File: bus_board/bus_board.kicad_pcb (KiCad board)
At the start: 2 copper layers, 150 x 30 mm, 20 parts, among them J5 Conn_02x08_Odd_Even, J6 Conn_02x08_Odd_Even, J7 Conn_02x08_Odd_Even, J8 Conn_02x08_Odd_Even

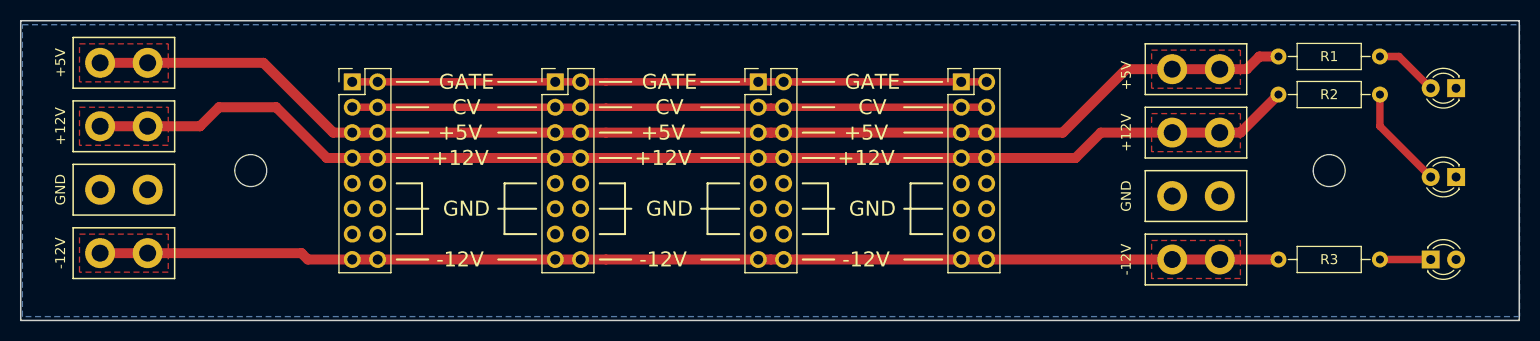
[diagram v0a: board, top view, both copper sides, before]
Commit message: added fuse holder
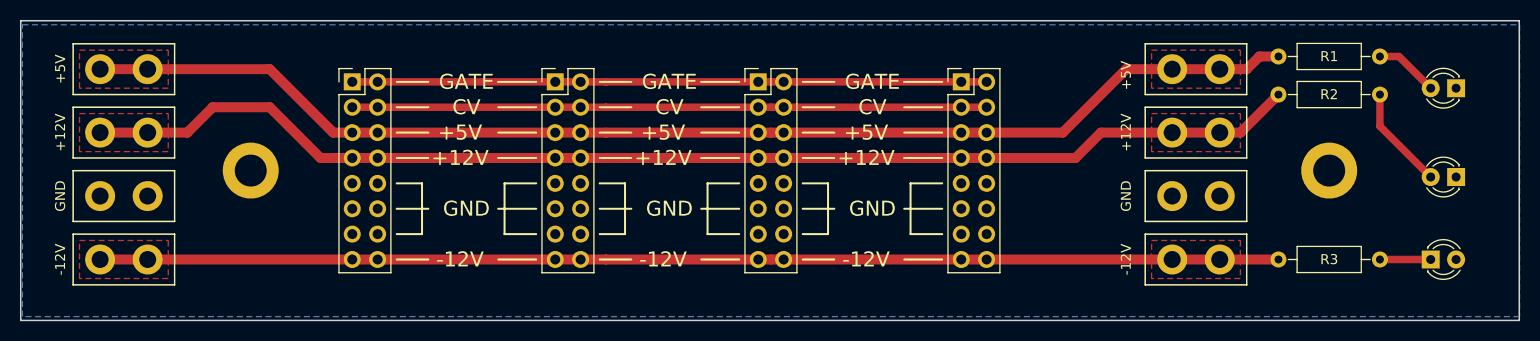
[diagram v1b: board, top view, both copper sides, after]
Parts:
- removed the REF** at (73.0, 80.0)
- removed the REF** at (181.0, 80.0)
- added REF**: MountingHole_3.2mm_M3_DIN965_Pad, Mounting_Holes:MountingHole_3.2mm_M3_DIN965_Pad, F.Cu at (181.0, 80.0)
- added REF**: MountingHole_3.2mm_M3_DIN965_Pad, Mounting_Holes:MountingHole_3.2mm_M3_DIN965_Pad, F.Cu at (73.0, 80.0)
- moved +12V 0.64 mm to (60.3, 77.5)
- moved +5V 0.64 mm to (60.3, 71.1)
- moved -12V 0.64 mm to (60.3, 90.2)
- moved GND 0.63 mm to (60.3, 83.8)
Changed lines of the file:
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@@
     (thickness 1.6)
     (drawings 79)
-    (tracks 70)
+    (tracks 68)
     (zones 0)
     (modules 20)
@@
     (visible_elements 7FFFFFFF)
     (pcbplotparams
-      (layerselection 0x010fc_ffffffff)
+      (layerselection 0x010f0_ffffffff)
       (usegerberextensions false)
       (usegerberattributes false)
@@
       (plotinvisibletext false)
       (padsonsilk false)
-      (subtractmaskfromsilk false)
+      (subtractmaskfromsilk true)
       (outputformat 1)
       (mirror false)
-      (drillshape 1)
+      (drillshape 0)
       (scaleselection 1)
-      (outputdirectory ""))
+      (outputdirectory "GERBERS/"))
   )
   (net 0 "")
@@
     (add_net /-12V)
   )
+  (module Mounting_Holes:MountingHole_3.2mm_M3_DIN965_Pad (layer F.Cu)
+    (at 180.975 80)
+    (descr "Mounting Hole 3.2mm, M3, DIN965")
+    (tags "mounting hole 3.2mm m3 din965")
+    (attr virtual)
+    (fp_text reference REF** (at 0 -3.8) (layer F.SilkS) hide
+      (effects (font (size 1 1) (thickness 0.15)))
+    )
+    (fp_text value MountingHole_3.2mm_M3_DIN965_Pad (at 0 3.8) (layer F.Fab)
+      (effects (font (size 1 1) (thickness 0.15)))
+    )
+    (fp_text user %R (at 0.3 0) (layer F.Fab)
+      (effects (font (size 1 1) (thickness 0.15)))
+    )
+    (fp_circle (center 0 0) (end 2.8 0) (layer Cmts.User) (width 0.15))
+    (fp_circle (center 0 0) (end 3.05 0) (layer F.CrtYd) (width 0.05))
+    (pad 1 thru_hole circle (at 0 0) (size 5.6 5.6) (drill 3.2) (layers *.Cu *.Mask))
+  )
   (module Pin_Headers:Pin_Header_Straight_2x08_Pitch2.54mm (layer F.Cu)
     (at 83.185 71.12)
@@
   )
   (module digikey-footprints:spade_connector (layer F.Cu)
-    (at 60.325 76.835)
+    (at 60.325 77.47)
     (fp_text reference +12V (at -6.35 -1.27 90) (layer F.SilkS)
       (effects (font (size 1 1) (thickness 0.15)))
@@
   )
   (module digikey-footprints:spade_connector (layer F.Cu)
-    (at 60.325 70.485)
+    (at 60.325 71.12)
     (fp_text reference +5V (at -6.35 -1.27 90) (layer F.SilkS)
       (effects (font (size 1 1) (thickness 0.15)))
@@
   )
   (module digikey-footprints:spade_connector (layer F.Cu)
-    (at 60.325 89.535)
+    (at 60.325 90.17)
     (fp_text reference -12V (at -6.35 -1.27 90) (layer F.SilkS)
       (effects (font (size 1 1) (thickness 0.15)))
@@
   )
   (module digikey-footprints:spade_connector (layer F.Cu)
-    (at 60.325 83.185)
+    (at 60.325 83.82)
     (fp_text reference GND (at -6.35 -1.27 90) (layer F.SilkS)
       (effects (font (size 1 1) (thickness 0.15)))
@@
       (net 1 /GND))
   )
-  (module Mounting_Holes:MountingHole_3.2mm_M3 (layer F.Cu)
+  (module Mounting_Holes:MountingHole_3.2mm_M3_DIN965_Pad (layer F.Cu)
     (at 73.025 80)
-    (descr "Mounting Hole 3.2mm, no annular, M3")
-    (tags "mounting hole 3.2mm no annular m3")
+    (descr "Mounting Hole 3.2mm, M3, DIN965")
+    (tags "mounting hole 3.2mm m3 din965")
     (attr virtual)
-    (fp_text reference REF** (at 0 -4.2) (layer F.SilkS) hide
-      (effects (font (size 1 1) (thickness 0.15)))
-    )
-    (fp_text value MountingHole_3.2mm_M3 (at 0 4.2) (layer F.Fab)
+    (fp_text reference REF** (at 0 -3.8) (layer F.SilkS) hide
+      (effects (font (size 1 1) (thickness 0.15)))
+    )
+    (fp_text value MountingHole_3.2mm_M3_DIN965_Pad (at 0 3.8) (layer F.Fab)
       (effects (font (size 1 1) (thickness 0.15)))
     )
@@
       (effects (font (size 1 1) (thickness 0.15)))
     )
-    (fp_circle (center 0 0) (end 3.2 0) (layer Cmts.User) (width 0.15))
-    (fp_circle (center 0 0) (end 3.45 0) (layer F.CrtYd) (width 0.05))
-    (pad 1 np_thru_hole circle (at 0 0) (size 3.2 3.2) (drill 3.2) (layers *.Cu *.Mask))
-  )
-  (module Mounting_Holes:MountingHole_3.2mm_M3 (layer F.Cu)
-    (at 180.975 80)
-    (descr "Mounting Hole 3.2mm, no annular, M3")
-    (tags "mounting hole 3.2mm no annular m3")
-    (attr virtual)
-    (fp_text reference REF** (at 0 -4.2) (layer F.SilkS) hide
-      (effects (font (size 1 1) (thickness 0.15)))
-    )
-    (fp_text value MountingHole_3.2mm_M3 (at 0 4.2) (layer F.Fab)
-      (effects (font (size 1 1) (thickness 0.15)))
-    )
-    (fp_text user %R (at 0.3 0) (layer F.Fab)
-      (effects (font (size 1 1) (thickness 0.15)))
-    )
-    (fp_circle (center 0 0) (end 3.2 0) (layer Cmts.User) (width 0.15))
-    (fp_circle (center 0 0) (end 3.45 0) (layer F.CrtYd) (width 0.05))
-    (pad 1 np_thru_hole circle (at 0 0) (size 3.2 3.2) (drill 3.2) (layers *.Cu *.Mask))
+    (fp_circle (center 0 0) (end 2.8 0) (layer Cmts.User) (width 0.15))
+    (fp_circle (center 0 0) (end 3.05 0) (layer F.CrtYd) (width 0.05))
+    (pad 1 thru_hole circle (at 0 0) (size 5.6 5.6) (drill 3.2) (layers *.Cu *.Mask))
   )
   (gr_line (start 138.43 71.12) (end 142.24 71.12) (layer F.SilkS) (width 0.2))
@@
   (gr_line (start 200 95) (end 200 65) (layer Edge.Cuts) (width 0.15))
   (gr_line (start 50 95) (end 200 95) (layer Edge.Cuts) (width 0.15))
-  (segment (start 57.945 88.265) (end 62.705 88.265) (width 1) (layer F.Cu) (net 2))
-  (segment (start 62.705 88.265) (end 78.105 88.265) (width 1) (layer F.Cu) (net 2))
-  (segment (start 78.74 88.9) (end 83.185 88.9) (width 1) (layer F.Cu) (net 2))
-  (segment (start 78.105 88.265) (end 78.74 88.9) (width 1) (layer F.Cu) (net 2))
   (segment (start 83.185 88.9) (end 85.725 88.9) (width 1) (layer F.Cu) (net 2))
   (segment (start 85.725 88.9) (end 106.045 88.9) (width 1) (layer F.Cu) (net 2))
@@
   (segment (start 165.26 88.9) (end 170.02 88.9) (width 1) (layer F.Cu) (net 2))
   (segment (start 170.02 88.9) (end 175.895 88.9) (width 1) (layer F.Cu) (net 2))
-  (segment (start 57.945 75.565) (end 62.705 75.565) (width 1) (layer F.Cu) (net 3))
-  (segment (start 80.645 78.74) (end 83.185 78.74) (width 1) (layer F.Cu) (net 3))
+  (segment (start 57.945 88.9) (end 62.705 88.9) (width 1) (layer F.Cu) (net 2))
+  (segment (start 62.705 88.9) (end 83.185 88.9) (width 1) (layer F.Cu) (net 2))
   (segment (start 83.185 78.74) (end 85.725 78.74) (width 1) (layer F.Cu) (net 3))
   (segment (start 85.725 78.74) (end 106.045 78.74) (width 1) (layer F.Cu) (net 3))
@@
   (segment (start 172.085 76.2) (end 175.895 72.39) (width 1) (layer F.Cu) (net 3))
   (segment (start 170.02 76.2) (end 172.085 76.2) (width 1) (layer F.Cu) (net 3))
-  (segment (start 80.645 78.74) (end 75.565 73.66) (width 1) (layer F.Cu) (net 3))
-  (segment (start 75.565 73.66) (end 69.85 73.66) (width 1) (layer F.Cu) (net 3))
-  (segment (start 69.85 73.66) (end 67.945 75.565) (width 1) (layer F.Cu) (net 3))
-  (segment (start 67.945 75.565) (end 62.705 75.565) (width 1) (layer F.Cu) (net 3))
-  (segment (start 57.945 69.215) (end 62.705 69.215) (width 1) (layer F.Cu) (net 4))
-  (segment (start 83.185 76.2) (end 81.28 76.2) (width 1) (layer F.Cu) (net 4))
-  (segment (start 81.28 76.2) (end 74.295 69.215) (width 1) (layer F.Cu) (net 4))
-  (segment (start 74.295 69.215) (end 62.705 69.215) (width 1) (layer F.Cu) (net 4))
+  (segment (start 83.185 78.74) (end 80.01 78.74) (width 1) (layer F.Cu) (net 3))
+  (segment (start 80.01 78.74) (end 74.93 73.66) (width 1) (layer F.Cu) (net 3))
+  (segment (start 74.93 73.66) (end 69.215 73.66) (width 1) (layer F.Cu) (net 3))
+  (segment (start 69.215 73.66) (end 66.675 76.2) (width 1) (layer F.Cu) (net 3))
+  (segment (start 66.675 76.2) (end 62.705 76.2) (width 1) (layer F.Cu) (net 3))
+  (segment (start 62.705 76.2) (end 57.945 76.2) (width 1) (layer F.Cu) (net 3))
   (segment (start 83.185 76.2) (end 85.725 76.2) (width 1) (layer F.Cu) (net 4))
   (segment (start 85.725 76.2) (end 106.045 76.2) (width 1) (layer F.Cu) (net 4))
@@
   (segment (start 172.72 69.85) (end 173.99 68.58) (width 1) (layer F.Cu) (net 4))
   (segment (start 173.99 68.58) (end 175.895 68.58) (width 1) (layer F.Cu) (net 4))
+  (segment (start 57.945 69.85) (end 62.705 69.85) (width 1) (layer F.Cu) (net 4))
+  (segment (start 62.705 69.85) (end 74.93 69.85) (width 1) (layer F.Cu) (net 4))
+  (segment (start 81.28 76.2) (end 83.185 76.2) (width 1) (layer F.Cu) (net 4))
+  (segment (start 74.93 69.85) (end 81.28 76.2) (width 1) (layer F.Cu) (net 4))
   (segment (start 187.96 68.58) (end 191.135 71.755) (width 0.75) (layer F.Cu) (net 5))
   (segment (start 186.055 68.58) (end 187.96 68.58) (width 0.75) (layer F.Cu) (net 5))
@@
     (polygon
       (pts
-        (xy 55.88 67.31) (xy 64.77 67.31) (xy 64.77 71.12) (xy 55.88 71.12)
+        (xy 55.88 67.945) (xy 64.77 67.945) (xy 64.77 71.755) (xy 55.88 71.755)
       )
     )
@@
     (polygon
       (pts
-        (xy 55.88 73.66) (xy 64.77 73.66) (xy 64.77 77.47) (xy 55.88 77.47)
+        (xy 55.88 74.295) (xy 64.77 74.295) (xy 64.77 78.105) (xy 55.88 78.105)
       )
     )
@@
     (polygon
       (pts
-        (xy 55.88 86.36) (xy 64.77 86.36) (xy 64.77 90.17) (xy 55.88 90.17)
+        (xy 55.88 86.995) (xy 64.77 86.995) (xy 64.77 90.805) (xy 55.88 90.805)
       )
     )
